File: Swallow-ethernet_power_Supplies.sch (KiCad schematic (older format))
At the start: 29 parts, among them P6 V_In, P7 +5V_In, U11 NCP1529, U12 NCP1529, U13 NCP303LSN09T1G

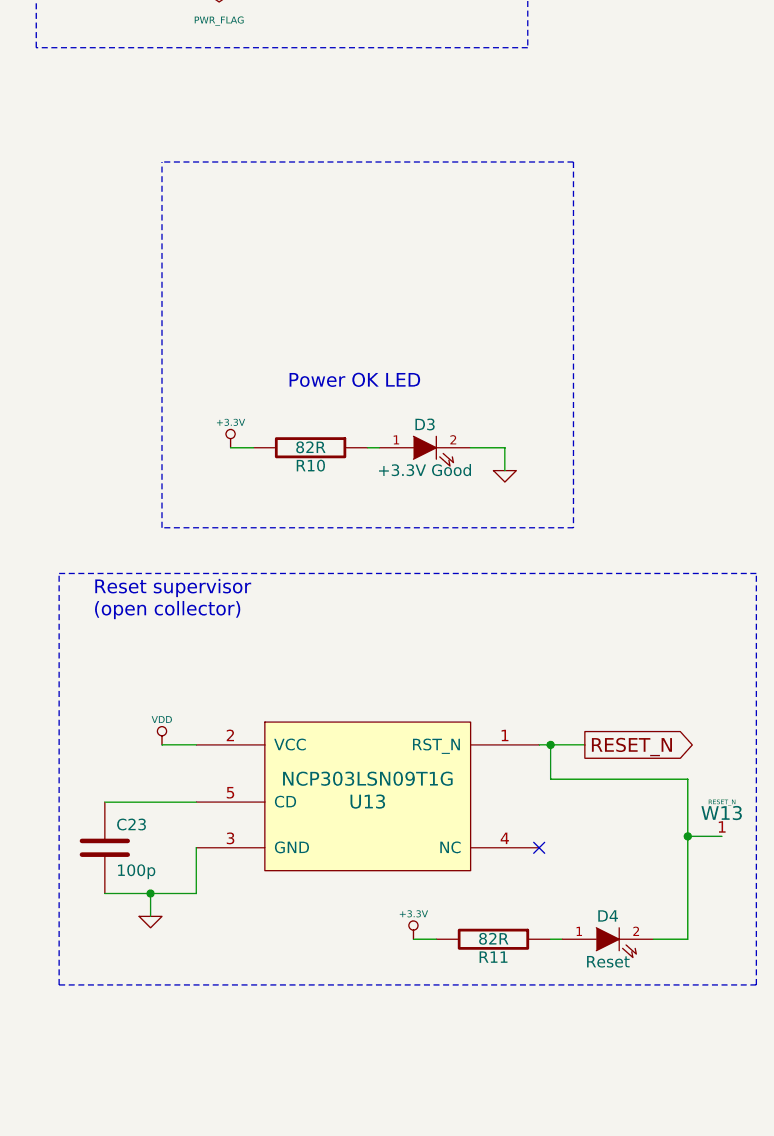
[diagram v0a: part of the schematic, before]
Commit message: Converted LED resistors from individuals to array. Connected most signals.
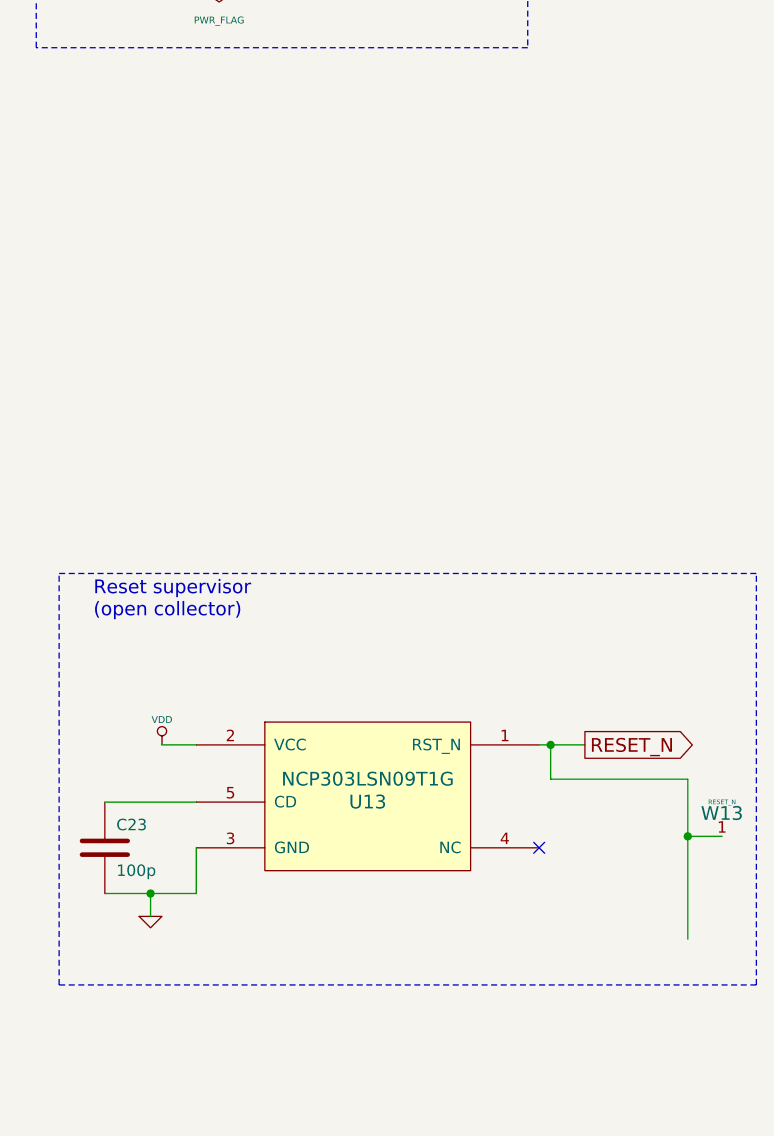
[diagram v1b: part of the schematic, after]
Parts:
- removed D3: +3.3V Good, X_LED-0603, symbol LED
- removed D4: Reset, X_LED-0603, symbol LED
- removed R10, R11: 82R, SM0402, symbol R
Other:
- note removed: "Power OK LED"
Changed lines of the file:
@@
-EESchema Schematic File Version 2  date 01/10/2012 17:33:27
+EESchema Schematic File Version 2  date Mon 01 Oct 2012 22:14:03 BST
 LIBS:power
 LIBS:device
@@
 Comment4 ""
 $EndDescr
-Text Notes 7950 4150 0    60   ~ 0
-Power OK LED
-Wire Wire Line
-	8900 4500 8900 4400
+Wire Wire Line
+	9700 6550 9700 5850
 Wire Wire Line
 	7650 2200 7650 2300
@@
 Wire Wire Line
 	9100 5850 9700 5850
-Wire Wire Line
-	9700 5850 9700 6550
 Wire Notes Line
 	6950 6750 6950 4950
@@
 Wire Wire Line
 	2400 6000 2300 6000
-Wire Notes Line
-	9200 3150 7400 3150
-Wire Notes Line
-	9200 3150 9200 4750
-Wire Notes Line
-	9200 4750 7400 4750
-Wire Notes Line
-	7400 4750 7400 3150
-Wire Wire Line
-	7700 4400 7800 4400
 Connection ~ 5650 5400
 Wire Wire Line
@@
 Connection ~ 5600 2000
 Wire Wire Line
-	8900 4400 8750 4400
-Wire Wire Line
-	8300 4400 8350 4400
-Wire Wire Line
 	7550 5950 7150 5950
 Wire Wire Line
 	7400 5700 7550 5700
-Wire Wire Line
-	9100 6550 9150 6550
-Wire Wire Line
-	9700 6550 9550 6550
-Wire Wire Line
-	8500 6550 8600 6550
 Wire Wire Line
 	9850 6100 9700 6100
@@
 $EndComp
 $Comp
-L +3.3V #PWR061
+L +3.3V #PWR063
 U 1 1 4F5FB6A5
 P 2300 5800
-F 0 "#PWR061" H 2300 5760 30  0001 C CNN
+F 0 "#PWR063" H 2300 5760 30  0001 C CNN
 F 1 "+3.3V" H 2300 5910 30  0000 C CNN
 	1    2300 5800
@@
 $EndComp
 $Comp
-L R R11
-U 1 1 4F5B50F0
-P 8850 6550
-F 0 "R11" V 8930 6550 50  0000 C CNN
-F 1 "82R" V 8850 6550 50  0000 C CNN
-F 2 "SM0402" H 8850 6550 60  0001 C CNN
-	1    8850 6550
-	0    1    1    0
-$EndComp
-$Comp
-L LED D4
-U 1 1 4F5B50EF
-P 9350 6550
-F 0 "D4" H 9350 6650 50  0000 C CNN
-F 1 "Reset" H 9350 6450 50  0000 C CNN
-F 2 "X_LED-0603" H 9350 6550 60  0001 C CNN
-	1    9350 6550
-	1    0    0    -1
-$EndComp
-$Comp
-L +3.3V #PWR062
-U 1 1 4F5B50EE
-P 8500 6550
-F 0 "#PWR062" H 8500 6510 30  0001 C CNN
-F 1 "+3.3V" H 8500 6660 30  0000 C CNN
-	1    8500 6550
-	1    0    0    -1
-$EndComp
-$Comp
-L VDD #PWR063
+L VDD #PWR064
 U 1 1 4ED160AA
 P 5800 5400
-F 0 "#PWR063" H 5800 5500 30  0001 C CNN
+F 0 "#PWR064" H 5800 5500 30  0001 C CNN
 F 1 "VDD" H 5800 5510 30  0000 C CNN
 	1    5800 5400
@@
 NoConn ~ 9050 6150
 $Comp
-L GND #PWR064
+L GND #PWR065
 U 1 1 4EDA727F
 P 7350 6450
-F 0 "#PWR064" H 7350 6450 30  0001 C CNN
+F 0 "#PWR065" H 7350 6450 30  0001 C CNN
 F 1 "GND" H 7350 6380 30  0001 C CNN
 	1    7350 6450
@@
 $EndComp
 $Comp
-L VDD #PWR065
+L VDD #PWR066
 U 1 1 4EDA7272
 P 7400 5700
-F 0 "#PWR065" H 7400 5800 30  0001 C CNN
+F 0 "#PWR066" H 7400 5800 30  0001 C CNN
 F 1 "VDD" H 7400 5810 30  0000 C CNN
 	1    7400 5700
@@
 $EndComp
 $Comp
-L GND #PWR066
-U 1 1 4ED17487
-P 8900 4500
-F 0 "#PWR066" H 8900 4500 30  0001 C CNN
-F 1 "GND" H 8900 4430 30  0001 C CNN
-	1    8900 4500
-	1    0    0    -1
-$EndComp
-$Comp
-L +3.3V #PWR067
-U 1 1 4ED17439
-P 7700 4400
-F 0 "#PWR067" H 7700 4360 30  0001 C CNN
-F 1 "+3.3V" H 7700 4510 30  0000 C CNN
-	1    7700 4400
-	1    0    0    -1
-$EndComp
-$Comp
-L LED D3
-U 1 1 4ED17411
-P 8550 4400
-F 0 "D3" H 8550 4500 50  0000 C CNN
-F 1 "+3.3V Good" H 8550 4300 50  0000 C CNN
-F 2 "X_LED-0603" H 8550 4400 60  0001 C CNN
-	1    8550 4400
-	1    0    0    -1
-$EndComp
-$Comp
-L R R10
-U 1 1 4ED17400
-P 8050 4400
-F 0 "R10" V 8130 4400 50  0000 C CNN
-F 1 "82R" V 8050 4400 50  0000 C CNN
-F 2 "SM0402" H 8050 4400 60  0001 C CNN
-	1    8050 4400
-	0    1    1    0
-$EndComp
-$Comp
-L PWR_FLAG #FLG068
+L PWR_FLAG #FLG067
 U 1 1 4ED16457
 P 5650 5100
-F 0 "#FLG068" H 5650 5370 30  0001 C CNN
+F 0 "#FLG067" H 5650 5370 30  0001 C CNN
 F 1 "PWR_FLAG" H 5650 5330 30  0000 C CNN
 	1    5650 5100
@@
 $EndComp
 $Comp
-L PWR_FLAG #FLG069
+L PWR_FLAG #FLG068
 U 1 1 4ED16447
 P 5600 1700
-F 0 "#FLG069" H 5600 1970 30  0001 C CNN
+F 0 "#FLG068" H 5600 1970 30  0001 C CNN
 F 1 "PWR_FLAG" H 5600 1930 30  0000 C CNN
 	1    5600 1700
@@
 $EndComp
 $Comp
-L PWR_FLAG #FLG070
+L PWR_FLAG #FLG069
 U 1 1 4ED162B6
 P 7650 2300
-F 0 "#FLG070" H 7650 2570 30  0001 C CNN
+F 0 "#FLG069" H 7650 2570 30  0001 C CNN
 F 1 "PWR_FLAG" H 7650 2530 30  0000 C CNN
 	1    7650 2300
@@
 $EndComp
 $Comp
-L PWR_FLAG #FLG071
+L PWR_FLAG #FLG070
 U 1 1 4ED16176
 P 7650 1900
-F 0 "#FLG071" H 7650 2170 30  0001 C CNN
+F 0 "#FLG070" H 7650 2170 30  0001 C CNN
 F 1 "PWR_FLAG" H 7650 2130 30  0000 C CNN
 	1    7650 1900
@@
 $EndComp
 $Comp
-L +5V #PWR072
+L +5V #PWR071
 U 1 1 4ED1613C
 P 7900 1900
-F 0 "#PWR072" H 7900 1990 20  0001 C CNN
+F 0 "#PWR071" H 7900 1990 20  0001 C CNN
 F 1 "+5V" H 7900 1990 30  0000 C CNN
 	1    7900 1900
@@
 $EndComp
 $Comp
-L GND #PWR073
+L GND #PWR072
 U 1 1 4ED16138
 P 7900 2350
-F 0 "#PWR073" H 7900 2350 30  0001 C CNN
+F 0 "#PWR072" H 7900 2350 30  0001 C CNN
 F 1 "GND" H 7900 2280 30  0001 C CNN
 	1    7900 2350
@@
 $EndComp
 $Comp
-L GND #PWR074
+L GND #PWR073
 U 1 1 4ED16054
 P 3150 6600
-F 0 "#PWR074" H 3150 6600 30  0001 C CNN
+F 0 "#PWR073" H 3150 6600 30  0001 C CNN
 F 1 "GND" H 3150 6530 30  0001 C CNN
 	1    3150 6600
@@
 $EndComp
 $Comp
-L +5V #PWR075
+L +5V #PWR074
 U 1 1 4ED1604D
 P 1750 5400
-F 0 "#PWR075" H 1750 5490 20  0001 C CNN
+F 0 "#PWR074" H 1750 5490 20  0001 C CNN
 F 1 "+5V" H 1750 5490 30  0000 C CNN
 	1    1750 5400
@@
 5V to 3.3V at 1A Step-down
 $Comp
-L +5V #PWR076
+L +5V #PWR075
 U 1 1 4ED15FDA
 P 1750 2000
-F 0 "#PWR076" H 1750 2090 20  0001 C CNN
+F 0 "#PWR075" H 1750 2090 20  0001 C CNN
 F 1 "+5V" H 1750 2090 30  0000 C CNN
 	1    1750 2000
@@
 $EndComp
 $Comp
-L +3.3V #PWR077
+L +3.3V #PWR076
 U 1 1 4ED15FB8
 P 5700 2000
-F 0 "#PWR077" H 5700 1960 30  0001 C CNN
+F 0 "#PWR076" H 5700 1960 30  0001 C CNN
 F 1 "+3.3V" H 5700 2110 30  0000 C CNN
 	1    5700 2000
@@
 $EndComp
 $Comp
-L GND #PWR078
+L GND #PWR077
 U 1 1 4ED15EEA
 P 3150 3200
-F 0 "#PWR078" H 3150 3200 30  0001 C CNN
+F 0 "#PWR077" H 3150 3200 30  0001 C CNN
 F 1 "GND" H 3150 3130 30  0001 C CNN
 	1    3150 3200

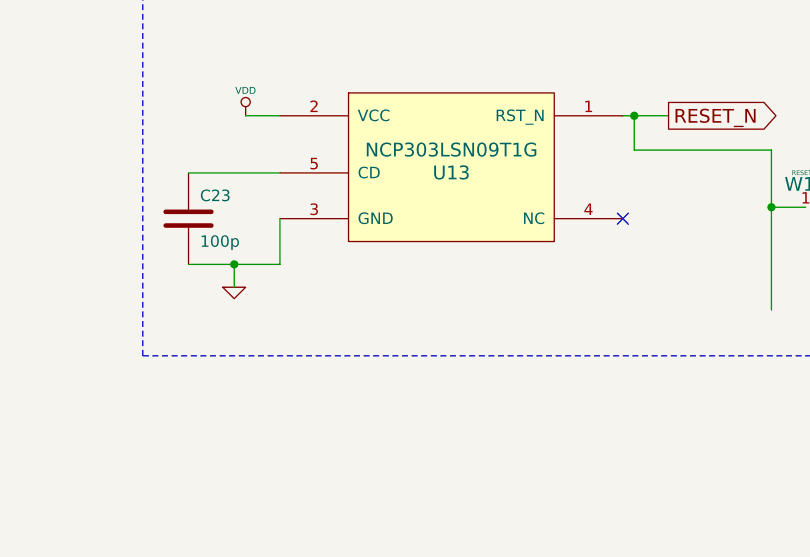
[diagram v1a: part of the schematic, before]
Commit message: Altered +5V capacitors to larger size for higher V rating. Changed reset chip cap from 100pF to 100nF to ensure a longer reset signal for the ethernet MAC.
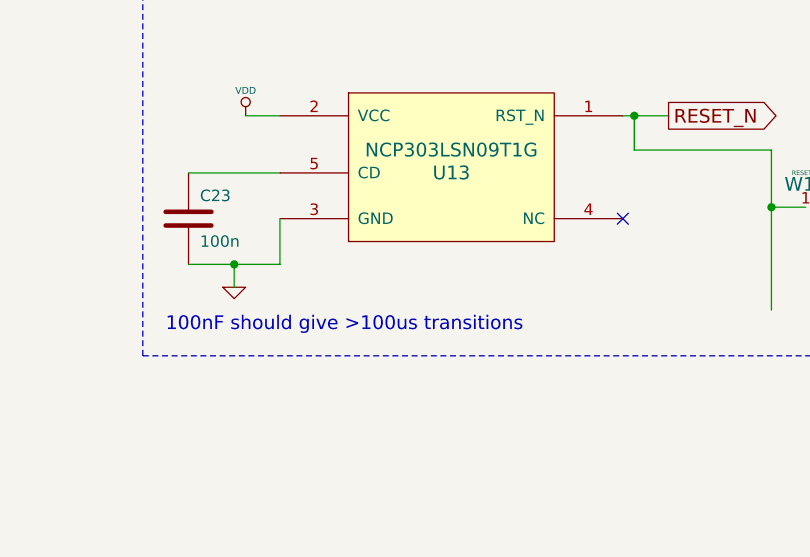
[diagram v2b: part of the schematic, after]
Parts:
- C23: value 100p -> 100n
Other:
- note added: "100nF should give >100us transitions"
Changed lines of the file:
@@
-EESchema Schematic File Version 2  date Mon 01 Oct 2012 22:14:03 BST
+EESchema Schematic File Version 2  date Tue 02 Oct 2012 10:45:58 BST
 LIBS:power
 LIBS:device
@@
 Sheet 4 4
 Title ""
-Date "1 oct 2012"
+Date "2 oct 2012"
 Rev ""
 Comp ""
@@
 Comment4 ""
 $EndDescr
+Text Notes 7050 6650 0    60   ~ 0
+100nF should give >100us transitions
 Wire Wire Line
 	9700 6550 9700 5850
@@
 $EndComp
 $Comp
-L +3.3V #PWR063
+L +3.3V #PWR064
 U 1 1 4F5FB6A5
 P 2300 5800
-F 0 "#PWR063" H 2300 5760 30  0001 C CNN
+F 0 "#PWR064" H 2300 5760 30  0001 C CNN
 F 1 "+3.3V" H 2300 5910 30  0000 C CNN
 	1    2300 5800
@@
 $EndComp
 $Comp
-L VDD #PWR064
+L VDD #PWR065
 U 1 1 4ED160AA
 P 5800 5400
-F 0 "#PWR064" H 5800 5500 30  0001 C CNN
+F 0 "#PWR065" H 5800 5500 30  0001 C CNN
 F 1 "VDD" H 5800 5510 30  0000 C CNN
 	1    5800 5400
@@
 NoConn ~ 9050 6150
 $Comp
-L GND #PWR065
+L GND #PWR066
 U 1 1 4EDA727F
 P 7350 6450
-F 0 "#PWR065" H 7350 6450 30  0001 C CNN
+F 0 "#PWR066" H 7350 6450 30  0001 C CNN
 F 1 "GND" H 7350 6380 30  0001 C CNN
 	1    7350 6450
@@
 $EndComp
 $Comp
-L VDD #PWR066
+L VDD #PWR067
 U 1 1 4EDA7272
 P 7400 5700
-F 0 "#PWR066" H 7400 5800 30  0001 C CNN
+F 0 "#PWR067" H 7400 5800 30  0001 C CNN
 F 1 "VDD" H 7400 5810 30  0000 C CNN
 	1    7400 5700
@@
 P 7150 6150
 F 0 "C23" H 7200 6250 50  0000 L CNN
-F 1 "100p" H 7200 6050 50  0000 L CNN
+F 1 "100n" H 7200 6050 50  0000 L CNN
 F 2 "SM0402" H 7150 6150 60  0001 C CNN
 	1    7150 6150
@@
 $EndComp
 $Comp
-L PWR_FLAG #FLG067
+L PWR_FLAG #FLG068
 U 1 1 4ED16457
 P 5650 5100
-F 0 "#FLG067" H 5650 5370 30  0001 C CNN
+F 0 "#FLG068" H 5650 5370 30  0001 C CNN
 F 1 "PWR_FLAG" H 5650 5330 30  0000 C CNN
 	1    5650 5100
@@
 $EndComp
 $Comp
-L PWR_FLAG #FLG068
+L PWR_FLAG #FLG069
 U 1 1 4ED16447
 P 5600 1700
-F 0 "#FLG068" H 5600 1970 30  0001 C CNN
+F 0 "#FLG069" H 5600 1970 30  0001 C CNN
 F 1 "PWR_FLAG" H 5600 1930 30  0000 C CNN
 	1    5600 1700
@@
 $EndComp
 $Comp
-L PWR_FLAG #FLG069
+L PWR_FLAG #FLG070
 U 1 1 4ED162B6
 P 7650 2300
-F 0 "#FLG069" H 7650 2570 30  0001 C CNN
+F 0 "#FLG070" H 7650 2570 30  0001 C CNN
 F 1 "PWR_FLAG" H 7650 2530 30  0000 C CNN
 	1    7650 2300
@@
 $EndComp
 $Comp
-L PWR_FLAG #FLG070
+L PWR_FLAG #FLG071
 U 1 1 4ED16176
 P 7650 1900
-F 0 "#FLG070" H 7650 2170 30  0001 C CNN
+F 0 "#FLG071" H 7650 2170 30  0001 C CNN
 F 1 "PWR_FLAG" H 7650 2130 30  0000 C CNN
 	1    7650 1900
@@
 $EndComp
 $Comp
-L +5V #PWR071
+L +5V #PWR072
 U 1 1 4ED1613C
 P 7900 1900
-F 0 "#PWR071" H 7900 1990 20  0001 C CNN
+F 0 "#PWR072" H 7900 1990 20  0001 C CNN
 F 1 "+5V" H 7900 1990 30  0000 C CNN
 	1    7900 1900
@@
 $EndComp
 $Comp
-L GND #PWR072
+L GND #PWR073
 U 1 1 4ED16138
 P 7900 2350
-F 0 "#PWR072" H 7900 2350 30  0001 C CNN
+F 0 "#PWR073" H 7900 2350 30  0001 C CNN
 F 1 "GND" H 7900 2280 30  0001 C CNN
 	1    7900 2350
@@
 $EndComp
 $Comp
-L GND #PWR073
+L GND #PWR074
 U 1 1 4ED16054
 P 3150 6600
-F 0 "#PWR073" H 3150 6600 30  0001 C CNN
+F 0 "#PWR074" H 3150 6600 30  0001 C CNN
 F 1 "GND" H 3150 6530 30  0001 C CNN
 	1    3150 6600
@@
 $EndComp
 $Comp
-L +5V #PWR074
+L +5V #PWR075
 U 1 1 4ED1604D
 P 1750 5400
-F 0 "#PWR074" H 1750 5490 20  0001 C CNN
+F 0 "#PWR075" H 1750 5490 20  0001 C CNN
 F 1 "+5V" H 1750 5490 30  0000 C CNN
 	1    1750 5400
@@
 5V to 3.3V at 1A Step-down
 $Comp
-L +5V #PWR075
+L +5V #PWR076
 U 1 1 4ED15FDA
 P 1750 2000
-F 0 "#PWR075" H 1750 2090 20  0001 C CNN
+F 0 "#PWR076" H 1750 2090 20  0001 C CNN
 F 1 "+5V" H 1750 2090 30  0000 C CNN
 	1    1750 2000
@@
 $EndComp
 $Comp
-L +3.3V #PWR076
+L +3.3V #PWR077
 U 1 1 4ED15FB8
 P 5700 2000
-F 0 "#PWR076" H 5700 1960 30  0001 C CNN
+F 0 "#PWR077" H 5700 1960 30  0001 C CNN
 F 1 "+3.3V" H 5700 2110 30  0000 C CNN
 	1    5700 2000
@@
 $EndComp
 $Comp
-L GND #PWR077
+L GND #PWR078
 U 1 1 4ED15EEA
 P 3150 3200
-F 0 "#PWR077" H 3150 3200 30  0001 C CNN
+F 0 "#PWR078" H 3150 3200 30  0001 C CNN
 F 1 "GND" H 3150 3130 30  0001 C CNN
 	1    3150 3200
